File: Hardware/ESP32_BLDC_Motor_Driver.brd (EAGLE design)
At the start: 85.1 x 57.1 mm, 175 parts, among them J1 USB-C Connector, J2 0532610371, J3 POWER_JACKPOWER_JACK_SLOT, J4 Breadboard Connector, J5 Breadboard Headers, J6 0.1in header, J7 QWIIC_RIGHT_ANGLE, J8 Breakout Header, Q1 20V/4.2A/52mΩ/1.4W, Q2 NPN Transistors, U1 TMC6300, U3 ESP-WROOM-3232D-NARROW, U4 CH340C, U5 ESD Diode, U6 AP63357, U7 AP2202-ADJ, U8 TMAG5273, U9 LMV324

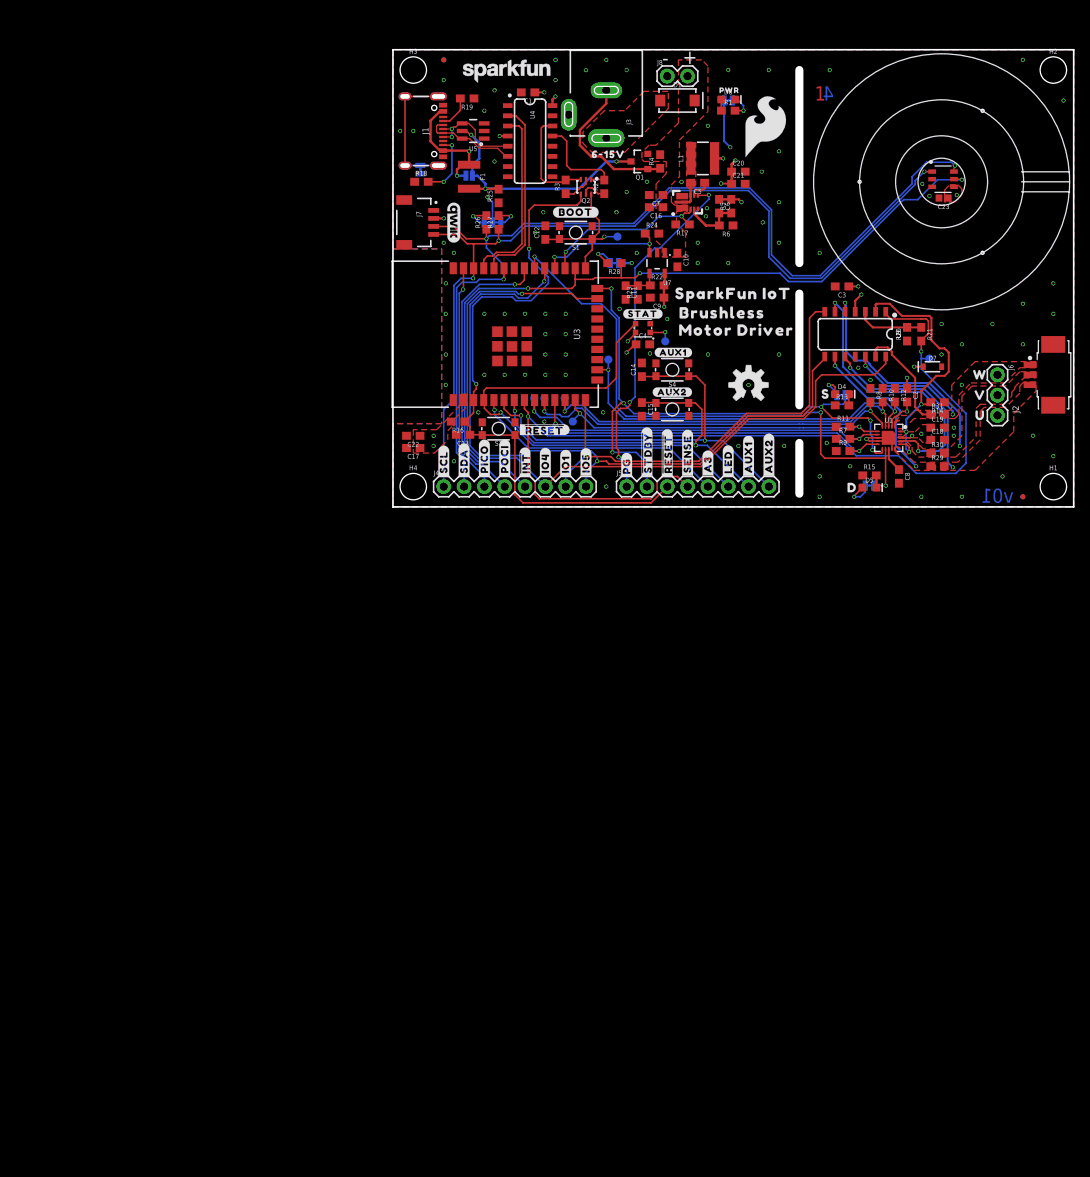
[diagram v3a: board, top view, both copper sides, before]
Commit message: Design Updates from design review - schematic changes mostly
***Changes are still not done*** Changes can be seen detailed in the protos design review; changed TMAG5273 symbol to be correct
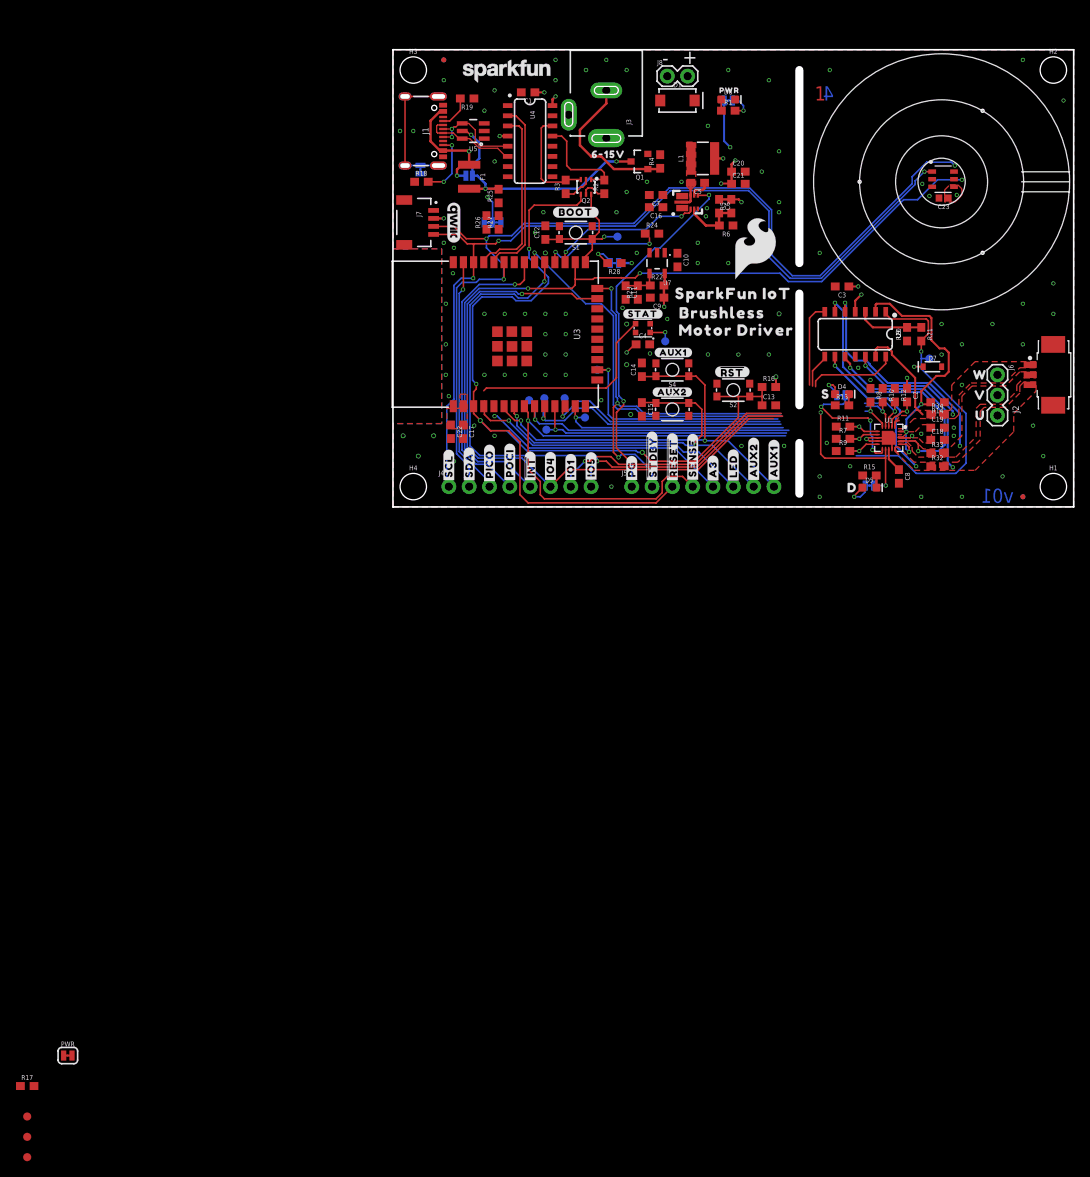
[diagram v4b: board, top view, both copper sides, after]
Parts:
- removed U$54: (no value), output:#_#RESET#630063003486
- added MOTOR: JUMPER-SMT_2_NC_TRACE_SILK, SparkFun-Jumpers:SMT-JUMPER_2_NC_TRACE_SILK
- added TP10, TP11, TP12: TEST-POINT3X4, SparkFun-Connectors:PAD.03X.04
- added U$63: (no value), output:##RST#630063003520
- J4, J5: device SparkFun-Connectors:1X08 -> SparkFun-Connectors:1X08_NO_SILK
- R17: value 100k -> 4.7k
- R32, R33, R34: value 0.015ohm -> 0.012ohm
- U3: value ESP-WROOM-3232D-NARROW -> ESP-WROOM-3232D; device SparkFun-RF:ESP-WROOM-32D-NARROW -> SparkFun-RF:ESP-WROOM-32D
- moved PWR 145.1 mm to (-40.6, -68.6), flipped to the top
- moved R17 135.3 mm to (-45.7, -72.4), turned to 0 degrees
- moved LOGO2 50.3 mm to (10.2, 52.1), flipped to the bottom
- moved R16 39.1 mm to (47.0, 15.0), turned to 0 degrees
- moved C13 38.4 mm to (47.0, 12.7), turned to 0 degrees
- moved S2 29.7 mm to (42.5, 14.6)
- moved LOGO3 15.3 mm to (45.3, 32.3)
- moved U$45 9.25 mm to (68.6, 36.8)
- moved C17 6.55 mm to (8.76, 9.40), turned to 270 degrees
- moved C22 4.73 mm to (7.24, 9.40), turned to 270 degrees
- moved U$8 3.22 mm to (47.6, 5.71)
- moved U$43 3.19 mm to (47.6, 5.84)
- moved U$9 1.97 mm to (45.1, 5.84)
- moved U$44 1.92 mm to (45.1, 5.97)
- moved TP3 1.89 mm to (25.5, 17.1)
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- renumbered R29 to R32, R30 to R33, R31 to R34
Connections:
- net ESP_4/!INT renamed ESP_4/!INT_MAG
- removed net 3.3V_LDO: C1.1, C17.1, C22.1, C23.1, C3.1, C4.1, C9.1, I2C.2, INT.2, J7.2, R16.2, R22.2, STAT.VCC, U3.2, U4.16, U4.4, U7.5, U8.4, U9.4
- removed net ESP_17/EN: R24.1, U3.28, U7.3
- new net 3.3V_A: C1.1, C17.1, C22.1, C23.1, C3.1, C4.1, C9.1, I2C.2, INT.2, J7.2, PWR.2, R16.2, R22.2, STAT.VCC, U3.2, U4.16, U4.4, U7.5, U8.4, U9.4
- new net ESP_12/LED: STAT.DI, U3.14
- new net ESP_17/________: U3.28
- new net ESP_36/V_OUT: U3.4, U9.7
- new net ESP_39/W_OUT: U3.5, U9.14
- new net LDO_EN: R24.1, U7.3
- new net N$10: R27.1, U8.6
- new net N$16: PWR.1, R17.2
- new net N$6: R26.1, U8.1
- net 3.3V: now also MOTOR.2; no longer PWR.2
- net ESP_12/V_OUT: now also TP11.1; no longer U3.14, U9.7
- net ESP_15/W_OUT: now also TP12.1; no longer U9.14
- net ESP_16/EN_MOTOR_PWR: no longer R17.1
- net ESP_21/TP_SDA: no longer R26.1, U8.6
- net ESP_22/TP_SCL: no longer R27.1, U8.1
- net ESP_36/LED: no longer STAT.DI, U3.4
- net ESP_39/TP_A3: no longer U3.5
- net ESP_5/U_OUT: now also TP10.1
- net GND: now also R17.1, U3.GND; no longer U3.GND1
- net N$12: now also R26.2; no longer R27.2
- net N$13: now also R27.2; no longer R26.2
- net N$23: now also MOTOR.1; no longer PWR.1
- net VIN: no longer R17.2
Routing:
- net !RESET: track 79.6 -> 124.2 mm, vias 2 -> 4
- net ESP_36/LED: track 62.0 -> 36.7 mm
- net ESP_12/LED: track 0.00 -> 25.0 mm
- net ESP_12/V_OUT: track 56.2 -> 31.8 mm
- net 3.3V_LDO: track 20.8 -> 0.00 mm, vias 14 -> 0
- net 3.3V_A: track 0.00 -> 20.6 mm, vias 0 -> 14
- net ESP_15/W_OUT: track 98.7 -> 79.0 mm
- net ESP_17/EN: track 16.6 -> 0.00 mm, vias 2 -> 0
- net ESP_17/________: track 0.00 -> 14.8 mm, vias 0 -> 2
- net ESP_27/VH: track 48.3 -> 36.0 mm
- net ESP_39/W_OUT: track 0.00 -> 11.3 mm
- net ESP_13/UH: track 48.1 -> 37.4 mm
- net ESP_36/V_OUT: track 0.00 -> 10.6 mm
- net ESP_32/CURR_SENSE: track 119.8 -> 109.2 mm
- net ESP_25/WH: track 49.8 -> 39.8 mm
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- added copper zone on layer 1, net 3.3V_A
- added copper zone on layer 15, net 3.3V_A
- removed copper zone on layer 15, net 3.3V
- removed copper zone on layer 1, net 3.3V_LDO
- removed copper zone on layer 15, net 3.3V_LDO
- removed copper zone on layer 1, net POWER_IN
- removed copper zone on layer 1, net VIN

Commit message: Updates for design review
Fixed schematic - reordering ESP_32 pinouts, breakout headers, adjusted inline current sensing; re-completed layout - repositioned placement of power scheme and input connectors, swapped placement of motor and motor driver/current sensors; fixed screw hole size of the motor; fixed schematic symbol for hall effect sensor.
For a full list, see design review document
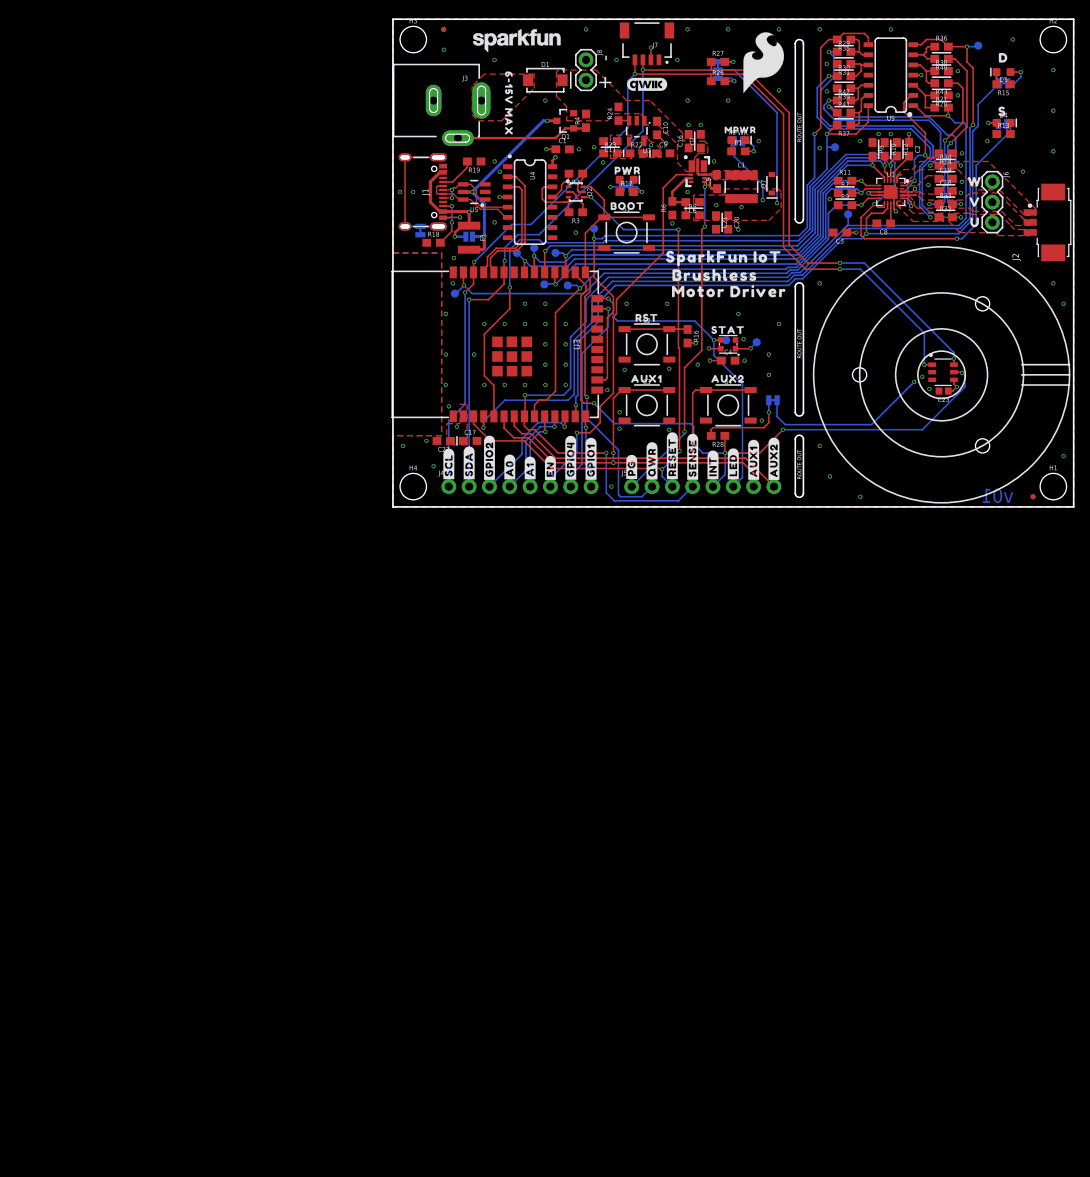
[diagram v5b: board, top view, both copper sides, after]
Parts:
- removed C12, C13, C14, C15: 0.1uF, SparkFun-Capacitors:0603
- removed D8: RED, SparkFun-LED:LED-0603
- removed R25: 10k, SparkFun-Resistors:0603
- added D2, MPWR: RED, SparkFun-LED:LED-0603
- added R29, R30, R40, R41, R42, R43: 20k, SparkFun-Resistors:0603
- added R31, R35, R36, R37, R38, R39: 1k, SparkFun-Resistors:0603
- added U$54: (no value), output:#27#GPIO2#27
- added U$64: (no value), output:#A0#30
- S1, S2, S3, S4: value MOMENTARY-SWITCH-SPST-SMD-4.6X2.8MM -> (none); device SparkFun-Switches:TACTILE_SWITCH_SMD_4.6X2.8MM -> SparkFun-Switches:TACTILE_SWITCH_SMD_5.2MM
- U$10: device output:#IO4#630063003461 -> output:#34#AUX2#21630063003531
- U$11: device output:#IO1#630063003461 -> output:BOOT21630063003532
- U$12: device output:#IO5#630063003461 -> output:PWR21630063003533
- U$13: device output:##INT#630063003461 -> output:#LED#630063003460
- U$14: device output:#POCI#630063003462 -> output:#AUX1#630063003461
- U$15: device output:#PICO#630063003463 -> output:#AUX2#630063003461
- U$16: device output:#SDA#630063003464 -> output:#2#LED#21630063003534
- U$17: device output:#SCL#630063003465 -> output:#4#INT_MAG#21630063003534
- U$18: device output:#AUX2#630063003471 -> output:#INT#8
- U$21: device output:#A3#630063003466 -> output:6#15V_MAX0
- U$22: device output:#AUX1#630063003471 -> output:#SENSE#9
- U$26: device output:#PWR#630063003472 -> output:#32#CURR_SENSE#10
- U$27: device output:#STAT#630063003470 -> output:#PWR#33
- U$29: device output:#_SCL#630063003479 -> output:#RESET#34
- U$3: device output:#PG#630063003456 -> output:AUX1630063003521
- U$30: device output:#_SDA#630063003480 -> output:#RESET#34
- U$31: device output:#_PICO#630063003481 -> output:#QWR#35
- U$32: device output:#_POCI#630063003482 -> output:#0#QWR#36
- U$33: device output:#_#INT#630063003483 -> output:#PG#30
- U$34: device output:#_IO4#630063003484 -> output:#GPIO1#4
- U$35: device output:#_IO1#630063003484 -> output:#12#GPIO1#4
- U$36: device output:#_IO2#630063003484 -> output:#GPIO4#13
- U$37: device output:#_PG#630063003484 -> output:#15#GPIO4#13
- U$38: device output:#_#STDBY#630063003485 -> output:#MOTOR_EN#16
- U$39: device output:#_#RESET#630063003486 -> output:#EN#17
- U$4: device output:##STDBY#630063003457 -> output:STAT1630063003522
- U$40: device output:#_SENSE#630063003487 -> output:#26#A0#30
- U$41: device output:#_A3#630063003488 -> output:#25#A1#30
- U$42: device output:#_LED#630063003488 -> output:#A1#30
- U$43: device output:#_AUX1#630063003489 -> output:#3V3_PG#31
- U$44: device output:#_AUX2#630063003489 -> output:#GPIO2#27
- U$5: device output:##RESET#630063003458 -> output:RST1630063003525
- U$55: device output:6#15V630063003510 -> output:#SDA#28
- U$56: device output:PWR3441 -> output:#21#SDA#29
- U$58: device output:#BOOT#630063003512 -> output:#SCL#29
- U$6: device output:#SENSE#630063003459 -> output:AUX21630063003526
- U$63: device output:##RST#630063003520 -> output:#22#SCL#30
- U$7: device output:#LED#630063003460 -> output:MPWR21630063003528
- U$8: device output:#AUX1#630063003461 -> output:#MPWR#21630063003530
- U$9: device output:#AUX2#630063003461 -> output:#35#AUX1#21630063003534
- moved TP11 180.9 mm to (73.2, 57.7), flipped to the bottom
- moved TP12 161.6 mm to (55.2, 45.0), flipped to the bottom
- moved R17 134.6 mm to (29.2, 39.4)
- moved TP10 131.7 mm to (25.1, 34.8), flipped to the bottom
- moved PWR 129.1 mm to (29.2, 40.0), flipped to the bottom
- moved U$53 57.0 mm to (76.3, 56.1)
- moved U$56 56.0 mm to (9.53, 6.48), flipped to the bottom, turned to 90 degrees
- moved D5 54.6 mm to (76.3, 54.4), turned to 180 degrees
- moved D 53.0 mm to (76.3, 53.0), turned to 0 degrees
- moved U$20 53.0 mm to (76.3, 54.6)
- moved U$21 52.4 mm to (14.5, 50.4), turned to 270 degrees
- moved R15 51.7 mm to (76.3, 52.8), turned to 180 degrees
- moved U$26 42.7 mm to (37.5, 10.0), turned to 90 degrees
- moved U$55 42.5 mm to (9.53, 5.33), turned to 90 degrees
- moved U$7 42.0 mm to (43.4, 47.1), turned to 0 degrees
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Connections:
- removed net ESP_0/!STDBY: J5.2, S.2, U1.11, U3.24
- removed net ESP_12/LED: STAT.DI, U3.14
- removed net ESP_12/V_OUT: J4.7, TP11.1
- removed net ESP_13/UH: R12.2, TP3.1, U1.3, U3.16
- removed net ESP_14/UL: R11.2, TP4.1, U1.6, U3.13
- removed net ESP_15/W_OUT: J4.6, TP12.1, U3.23
- removed net ESP_16/EN_MOTOR_PWR: U3.27, U6.P$2
- removed net ESP_17/________: U3.28
- removed net ESP_18/DIAG: D.2, U1.12, U3.30
- removed net ESP_19/POCI: J4.4, U3.31
- removed net ESP_23/PICO: J4.3, U3.37
- removed net ESP_25/WH: R8.2, TP7.1, U1.5, U3.10
- removed net ESP_26/VL: R9.2, TP6.1, U1.10, U3.11
- removed net ESP_27/VH: R10.2, TP5.1, U1.4, U3.12
- removed net ESP_36/LED: J5.6
- removed net ESP_39/TP_A3: J5.5
- removed net ESP_5/U_OUT: J4.8, TP10.1, U3.29, U9.8
- removed net N$10: R27.1, U8.6
- removed net N$6: R26.1, U8.1
- new net ESP_12/GPIO1: J4.8, U3.14
- new net ESP_13/U_OUT: R35.2, TP10.1, U3.16, U9.8
- new net ESP_14/DIAG: D.2, U1.12, U3.13
- new net ESP_15/GPIO4: J4.7, U3.23
- new net ESP_16/UH: R12.2, TP3.1, U1.3, U3.27
- new net ESP_17/UL: R11.2, TP4.1, U1.6, U3.28
- new net ESP_18/VH: R10.2, TP5.1, U1.4, U3.30
- new net ESP_19/WH: R8.2, TP7.1, U1.5, U3.31
- new net ESP_2/RGB_DI: J5.6, STAT.DI, TP1.1, U3.24
- new net ESP_23/VL: R9.2, TP6.1, U1.10, U3.37
- new net ESP_25/TP_A1: J4.5, U3.10
- new net ESP_26/TP_A0: J4.4, U3.11
- new net ESP_27/GPIO2: J4.3, U3.12
- new net ESP_5/!STDBY: S.2, U1.11, U3.29
- new net MOTOR_EN: J4.6, U6.P$2
- new net N$16: R29.2, R35.1, U9.9
- new net N$18: R30.2, R31.1, U9.10
- new net N$19: R36.1, R40.2, U9.6
- new net N$20: R38.1, R43.2, U9.5
- new net N$24: R37.1, R41.2, U9.13
- new net N$25: R39.1, R42.2, U9.12
- new net N$9: D2.A, R17.1
- net !RESET: now also S2.1, S2.2; no longer C13.1, S2.3, S2.4
- net 3.3V: now also C23.1, C3.1, I2C.2, INT.2, U8.4, U9.4
- net 3.3V_A: no longer C23.1, C3.1, I2C.2, INT.2, U8.4, U9.4
- net ESP_0/QPWR: now also J5.2, S1.1, S1.2; no longer C12.1, S1.3, S1.4, TP1.1
- net ESP_21/TP_SDA: now also R27.1, U8.6
- net ESP_22/TP_SCL: now also R26.1, U8.1
- net ESP_34/AUX1: now also J5.7, S3.1, S3.2; no longer C14.1, J5.8, S4.3, S4.4
- net ESP_35/AUX2: now also J5.8, S4.1, S4.2; no longer C15.1, J5.7, S3.3, S3.4
- net ESP_36/V_OUT: now also R36.2, TP11.1
- net ESP_39/W_OUT: now also R37.2, TP12.1
- net ESP_4/!INT_MAG: now also J5.5; no longer J4.5
- net GND: now also D2.C, J3.GND, MPWR.C, R31.2, R38.2, R39.2, S1.3, S1.4, S2.3, S2.4, S3.3, S3.4, S4.3, S4.4; no longer C12.2, C13.2, C14.2, C15.2, D8.C, J3.GNDBREAK, R17.1, R25.1, S1.1, S1.2, S2.1, S2.2, S3.1, S3.2, S4.1, S4.2
- net N$34: now also MPWR.A; no longer D8.A
- net N$5: now also J3.GNDBREAK; no longer J3.GND
- net SENSE_U: now also R30.1; no longer U9.9
- net SENSE_V: now also R43.1; no longer U9.6
- net SENSE_W: now also R42.1; no longer U9.13
- net U: now also R29.1; no longer U9.10
- net V: now also R40.1; no longer U9.5
- net V_USB: no longer R25.2
- net W: now also R41.1; no longer U9.12
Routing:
- net ESP_36/V_OUT: track 10.6 -> 109.8 mm, vias 0 -> 3
- net ESP_5/!STDBY: track 0.00 -> 97.3 mm, vias 0 -> 3
- net ESP_14/DIAG: track 0.00 -> 90.7 mm, vias 0 -> 2
- net ESP_5/U_OUT: track 81.8 -> 0.00 mm, vias 2 -> 0
- net ESP_13/U_OUT: track 0.00 -> 79.5 mm, vias 0 -> 2
- net ESP_15/W_OUT: track 79.0 -> 0.00 mm, vias 1 -> 0
- net ESP_39/W_OUT: track 11.3 -> 84.8 mm, vias 0 -> 2
- net ESP_0/!STDBY: track 68.4 -> 0.00 mm, vias 6 -> 0
- net ESP_18/DIAG: track 66.9 -> 0.00 mm, vias 3 -> 0
- net ESP_23/VL: track 0.00 -> 63.6 mm, vias 0 -> 2
- net ESP_18/VH: track 0.00 -> 59.1 mm, vias 0 -> 2
- net ESP_19/WH: track 0.00 -> 58.7 mm, vias 0 -> 2
- net ESP_16/UH: track 0.00 -> 56.2 mm, vias 0 -> 2
- net ESP_17/UL: track 0.00 -> 53.5 mm, vias 0 -> 2
- net MOTOR_EN: track 0.00 -> 48.3 mm, vias 0 -> 1
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- added copper zone on layer 15, net 3.3V
- added copper zone on layer 1, net N$2
- added copper zone on layer 1, net POWER_IN
- added copper zone on layer 1, net VIN
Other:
- board size 85.1 x 57.1 mm -> 85.1 x 61 mm
- board text added: "1.6mm Thickness 4-Layer 1oz copper outer 0.5oz copper inner Lead Free HASL"
- board text added: "ROUTE OUT"
- board text removed: "1"
- board text removed: "2"
- board text removed: "3"
- board text removed: "4"
- board text removed: "Board thickness is 1.6mm 4-Layer 1oz copper outer 0.5oz copper inner"
